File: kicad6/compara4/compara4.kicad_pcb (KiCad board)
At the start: 2 copper layers, 74.7 x 106.5 mm, 67 parts, among them J1 In_1, J2 In_2, J3 In_3, J4 In_4, J5 CV_Jack, J6 Out_OR, J7 Out_NOR, J8 Out_XOR, J9 Out_XNOR, Q1 BC547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

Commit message: notes, some design bits, state of progress
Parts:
- moved U3 151.7 mm to (248.9, 106.7)
- moved U2 139.4 mm to (248.9, 78.7)
- moved U1 127.0 mm to (248.9, 48.3)
- moved R14 74.2 mm to (193.6, 139.3)
- moved D5 74.2 mm to (197.3, 126.9)
- moved Q1 74.2 mm to (190.5, 152.4)
- moved Q2 74.2 mm to (219.7, 119.3)
- moved Q4 74.2 mm to (211.1, 131.4)
- moved R28 74.2 mm to (193.6, 135.3)
- moved R31 74.2 mm to (208.1, 127.2)
- moved R34 74.2 mm to (186.5, 127.2)
- moved Q3 74.2 mm to (205.2, 137.0)
- moved R11 74.2 mm to (186.5, 123.1)
- moved R13 74.2 mm to (208.1, 119.1)
- moved R15 74.2 mm to (186.5, 119.1)
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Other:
- board size 74.7 x 106.5 mm -> 239.4 x 106.5 mm

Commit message: compara4; breakout controls, layout for perfboard
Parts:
- removed D11: LED_XOR, LED_THT:LED_D3.0mm_FlatTop
- removed D12: LED_XNOR, LED_THT:LED_D3.0mm_FlatTop
- removed Q1, Q2, Q3, Q4: BC547, Package_TO_SOT_THT:TO-92_Inline
- removed R22, R23, R24: 10k, Resistor_THT:R_Axial_DIN0207_L6.3mm_D2.5mm_P7.62mm_Horizontal
- added C4: 10uF, Capacitor_THT:CP_Radial_D5.0mm_P2.50mm, F.Cu at (172.7, 129.6)
- added C5: 10uF, Capacitor_THT:CP_Radial_D5.0mm_P2.50mm, F.Cu at (172.7, 121.9)
- added J10: In_4, Connector_Audio:Jack_3.5mm_QingPu_WQP-PJ398SM_Vertical_CircularHoles, F.Cu at (86.4, 85.1)
- added J11: CV_Jack, Connector_Audio:Jack_3.5mm_QingPu_WQP-PJ398SM_Vertical_CircularHoles, F.Cu at (86.4, 54.6)
- added J12: Conn_02x05_Top_Bottom, Connector_IDC:IDC-Header_2x05_P2.54mm_Vertical, F.Cu at (182.9, 132.1)
- D10: value LED_NOR -> LED_Dual_Bidirectional; footprint LED_THT:LED_D3.0mm_FlatTop -> LED_THT:LED_D5.0mm
- D9: value LED_OR -> LED_Dual_Bidirectional; footprint LED_THT:LED_D3.0mm_FlatTop -> LED_THT:LED_D5.0mm
- J1: value In_1 -> Conn_01x34_Female; footprint Connector_Audio:Jack_3.5mm_QingPu_WQP-PJ398SM_Vertical_CircularHoles -> Connector_PinHeader_2.54mm:PinHeader_1x34_P2.54mm_Vertical; moved to B.Cu
- J2: value In_2 -> Conn_01x34_Male; footprint Connector_Audio:Jack_3.5mm_QingPu_WQP-PJ398SM_Vertical_CircularHoles -> Connector_PinHeader_2.54mm:PinHeader_1x34_P2.54mm_Horizontal; moved to B.Cu
- J3: value In_3 -> In_1
- J4: value In_4 -> In_2
- J5: value CV_Jack -> In_3
- J6: value Out_OR -> Out_XOR
- J7: value Out_NOR -> Out_XNOR
- J8: value Out_XOR -> Out_OR
- J9: value Out_XNOR -> Out_NOR
- R1: value 100k -> 10k
- R12: value 100k -> 47k
- R2, R21: value 10k -> 100k
- R7: value 47k -> 100k
- moved R12 131.4 mm to (68.6, 53.3), turned to -90 degrees
- moved R21 117.9 mm to (86.4, 40.6), turned to -90 degrees
- moved U3 112.1 mm to (139.7, 132.1), turned to 90 degrees
- moved R25 110.9 mm to (118.1, 119.4)
- moved R13 110.3 mm to (125.7, 45.7)
- moved U1 106.7 mm to (142.2, 45.7)
- moved R26 103.7 mm to (118.1, 134.6)
- moved R9 103.4 mm to (129.5, 55.9), turned to 90 degrees
- moved R14 94.0 mm to (134.6, 66.0)
- moved R17 89.8 mm to (133.3, 99.1), turned to 90 degrees
- moved R16 89.7 mm to (166.4, 45.7), turned to 180 degrees
- moved R2 89.5 mm to (118.1, 71.1), turned to 90 degrees
- moved D8 89.1 mm to (137.2, 96.5), turned to 90 degrees
- moved R3 88.7 mm to (123.2, 59.7), turned to -90 degrees
- moved U2 82.5 mm to (166.4, 78.7)
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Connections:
- D10 pad 1: Net-(D10-Pad1) -> /controls/LED_XOR_+
- D10 pad 2: Net-(D10-Pad2) -> /controls/LED_XOR_-
- D9 pad 1: Net-(D10-Pad2) -> /controls/LED_OR_+
- D9 pad 2: Net-(D10-Pad1) -> /controls/LED_OR_-
- J3 pad T: Net-(J3-PadT) -> /controls/IN1
- J4 pad T: Net-(J4-PadT) -> /controls/IN2
- J5 pad T: Net-(J5-PadT) -> /controls/IN3
- J5 pad TN: Net-(J5-PadTN) -> GND
- J6 pad T: Net-(J6-PadT) -> /controls/XOR
- J7 pad T: Net-(J7-PadT) -> /controls/XNOR
- J8 pad T: Net-(J8-PadT) -> /controls/OR
- J9 pad T: Net-(J9-PadT) -> /controls/NOR
- R1 pad 1: Net-(J5-PadTN) -> Net-(J2-Pad3)
- R12 pad 2: GND -> Net-(J11-PadT)
- R2 pad 2: Net-(J5-PadTN) -> Net-(J2-Pad3)
- R21 pad 1: Net-(Q1-Pad2) -> Net-(R12-Pad1)
- R21 pad 2: Net-(R21-Pad2) -> GND
- R25 pad 1: Net-(R25-Pad1) -> /LED_OR_-
- R25 pad 2: Net-(D10-Pad2) -> Net-(R25-Pad2)
- R26 pad 1: Net-(R26-Pad1) -> /LED_XOR_-
- R26 pad 2: Net-(D11-Pad1) -> Net-(R26-Pad2)
- R27 pad 1: Net-(J6-PadT) -> /OR
- R27 pad 2: Net-(Q1-Pad3) -> Net-(R27-Pad2)
- R28 pad 1: Net-(J7-PadT) -> /NOR
- R28 pad 2: Net-(Q2-Pad3) -> Net-(R28-Pad2)
- R29 pad 1: Net-(J6-PadT) -> /OR
- R3 pad 2: Net-(J1-PadT) -> Net-(J2-Pad11)
- R30 pad 1: Net-(J7-PadT) -> /NOR
- R31 pad 1: Net-(J8-PadT) -> /XOR
- R31 pad 2: Net-(Q3-Pad3) -> Net-(R31-Pad2)
- R32 pad 1: Net-(J9-PadT) -> /XNOR
- R32 pad 2: Net-(Q4-Pad3) -> Net-(R32-Pad2)
- R33 pad 1: Net-(J8-PadT) -> /XOR
- R34 pad 1: Net-(J9-PadT) -> /XNOR
- R4 pad 2: Net-(J2-PadT) -> Net-(J2-Pad12)
- R5 pad 2: Net-(J3-PadT) -> Net-(J2-Pad17)
- R6 pad 2: Net-(J4-PadT) -> Net-(J2-Pad18)
- R7 pad 1: Net-(R12-Pad1) -> Net-(D5-Pad1)
- R7 pad 2: Net-(J5-PadT) -> GND
- RV1 pad 2: Net-(RV1-Pad2) -> /controls/Threshold
- SW1 pad 1: +12V -> /controls/+12V
- SW1 pad 2: Net-(SW1-Pad2) -> /controls/Switch
- U1 pad 13: Net-(RV1-Pad2) -> /Threshold
- U1 pad 2: Net-(RV1-Pad2) -> /Threshold
- U1 pad 6: Net-(RV1-Pad2) -> /Threshold
- U1 pad 9: Net-(RV1-Pad2) -> /Threshold
- U2 pad 13: Net-(SW1-Pad2) -> /Switch
- U3 pad 1: Net-(D11-Pad2) -> /LED_XOR_+
- U3 pad 11: Net-(R21-Pad2) -> Net-(R27-Pad2)
- U3 pad 12: Net-(R22-Pad2) -> Net-(R28-Pad2)
- U3 pad 2: Net-(R26-Pad1) -> Net-(R26-Pad2)
- U3 pad 4: Net-(R23-Pad2) -> Net-(R31-Pad2)
- U3 pad 5: Net-(R24-Pad2) -> Net-(R32-Pad2)
- U3 pad 8: Net-(D10-Pad1) -> /LED_OR_+
- U3 pad 9: Net-(R25-Pad1) -> Net-(R25-Pad2)
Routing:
- net GND: track 0.00 -> 652.0 mm, vias 0 -> 6
- net +12V: track 0.00 -> 249.5 mm, vias 0 -> 2
- net -12V: track 0.00 -> 160.0 mm, vias 0 -> 2
- net /Switch: track 0.00 -> 100.3 mm
- net Net-(D5-Pad1): track 0.00 -> 88.9 mm, vias 0 -> 7
- net Net-(J2-Pad18): track 0.00 -> 88.9 mm
- net Net-(U2-Pad10): track 0.00 -> 86.4 mm, vias 0 -> 4
- net Net-(J2-Pad17): track 0.00 -> 76.2 mm
- net /Threshold: track 0.00 -> 58.4 mm
- net /LED_OR_+: track 0.00 -> 48.3 mm, vias 0 -> 1
- net Net-(D4-Pad1): track 0.00 -> 47.0 mm, vias 0 -> 3
- net Net-(D1-Pad1): track 0.00 -> 45.7 mm
- net Net-(D4-Pad2): track 0.00 -> 43.5 mm, vias 0 -> 4
- net Net-(D1-Pad2): track 0.00 -> 43.4 mm, vias 0 -> 2
- net Net-(R13-Pad1): track 0.00 -> 43.2 mm, vias 0 -> 4
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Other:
- board size 239.4 x 106.5 mm -> 124 x 106.5 mm

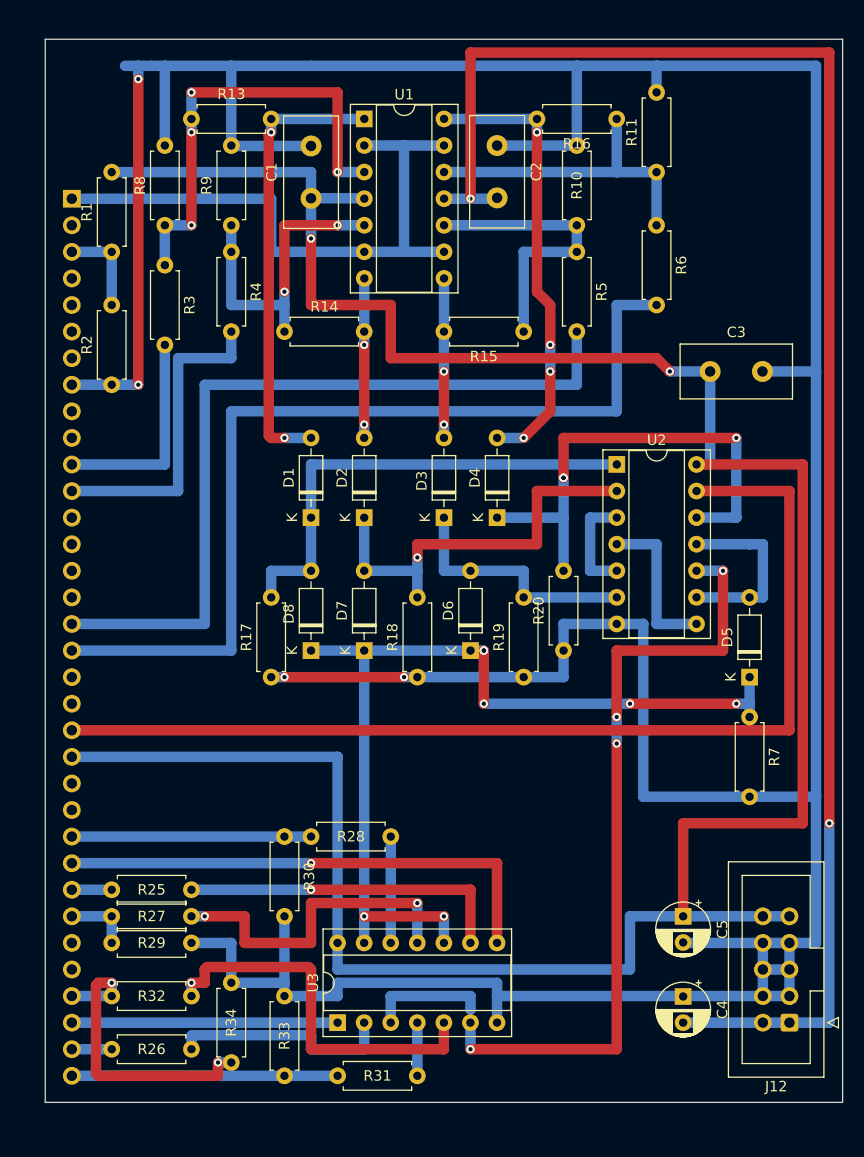
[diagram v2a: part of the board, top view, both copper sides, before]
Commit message: compara4 routing corrections: 2.54mm grid
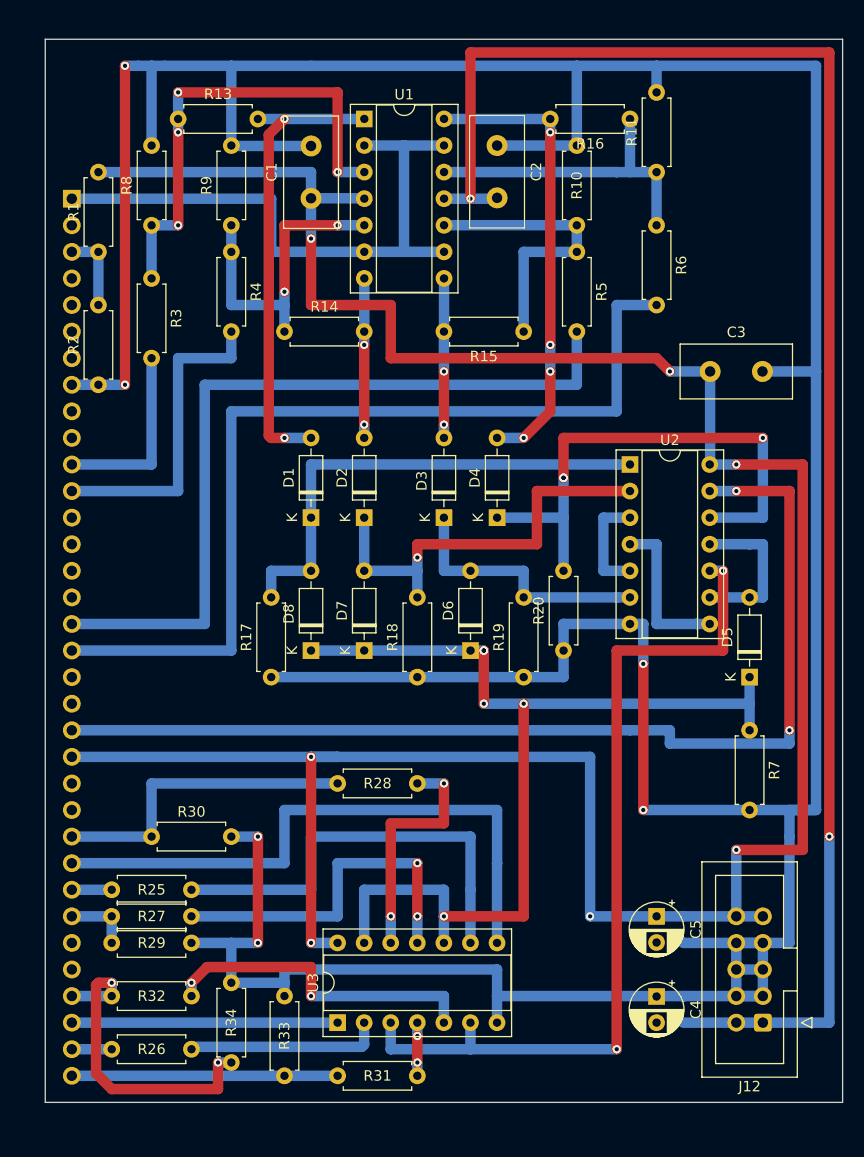
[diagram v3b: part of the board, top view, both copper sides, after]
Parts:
- moved R30 12.7 mm to (121.9, 114.3), turned to 0 degrees
- moved R28 5.68 mm to (139.7, 109.2)
- moved C4 2.54 mm to (170.2, 129.6)
- moved C5 2.54 mm to (170.2, 121.9)
- moved J12 2.54 mm to (180.3, 132.1)
- moved R3 1.80 mm to (121.9, 61.0)
- moved R13 1.27 mm to (124.5, 45.7)
- moved R1 1.27 mm to (116.8, 58.4)
- moved R2 1.27 mm to (116.8, 71.1)
- moved R7 1.27 mm to (179.1, 104.1)
- moved R8 1.27 mm to (121.9, 55.9)
- moved R16 1.27 mm to (167.6, 45.7)
- moved U2 1.26 mm to (167.6, 78.7)
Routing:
- net GND: track 652.0 -> 664.7 mm, vias 6 -> 8
- net Net-(R28-Pad2): track 10.2 -> 22.9 mm, vias 0 -> 2
- net Net-(R25-Pad2): track 31.8 -> 41.9 mm, vias 1 -> 0
- net /LED_OR_+: track 48.3 -> 58.4 mm, vias 1 -> 0
- net Net-(D5-Pad1): track 88.9 -> 97.8 mm, vias 7 -> 5
- net /NOR: track 22.9 -> 30.5 mm
- net Net-(R32-Pad2): track 37.0 -> 31.3 mm, vias 1 -> 2
- net Net-(D4-Pad1): track 47.0 -> 50.8 mm
- net +12V: track 249.5 -> 253.3 mm, vias 2 -> 7
- net Net-(R26-Pad2): track 21.7 -> 18.8 mm
- net Net-(R27-Pad2): track 31.7 -> 34.3 mm
- net Net-(R13-Pad1): track 43.2 -> 45.7 mm
- net Net-(J2-Pad11): track 20.3 -> 17.8 mm
- net Net-(U2-Pad10): track 86.4 -> 83.8 mm, vias 4 -> 2
- net Net-(D5-Pad2): track 17.8 -> 15.2 mm
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
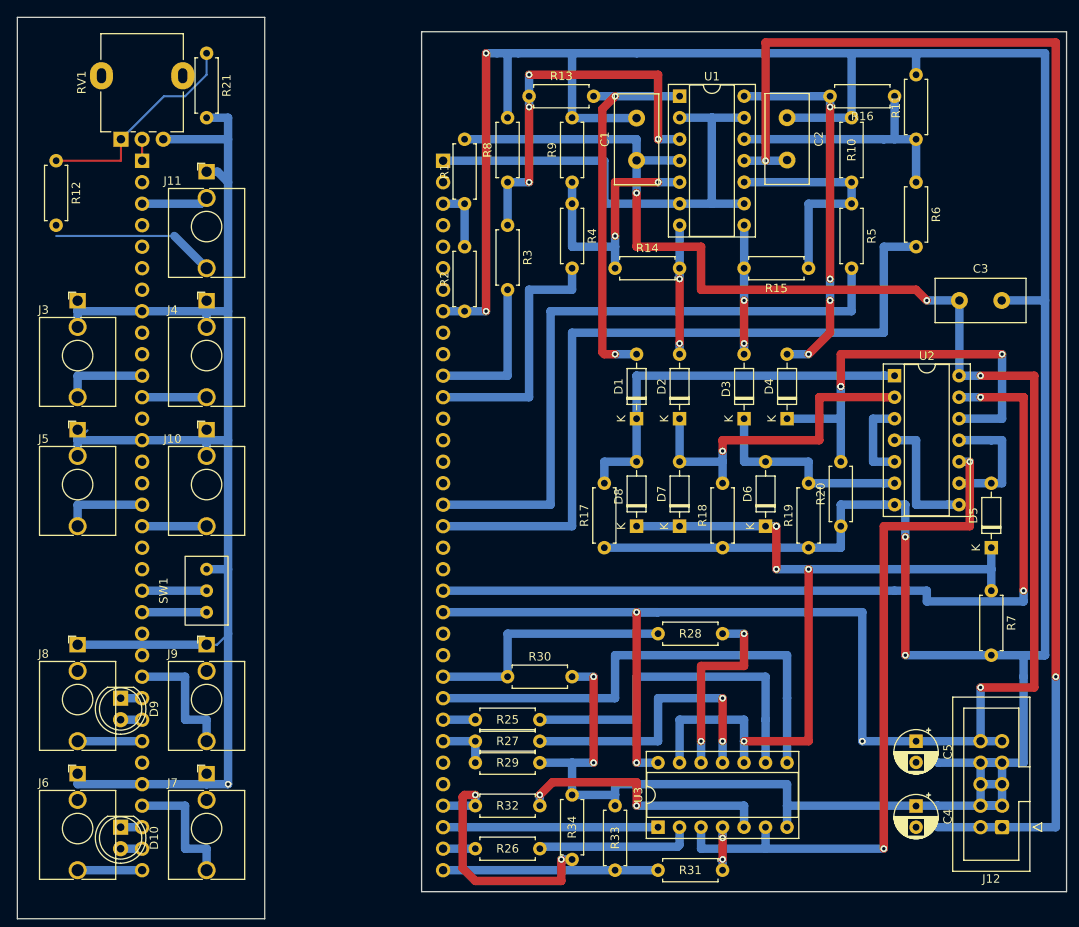
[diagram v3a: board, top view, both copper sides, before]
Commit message: compara4: reverse pot and cleanup ERC
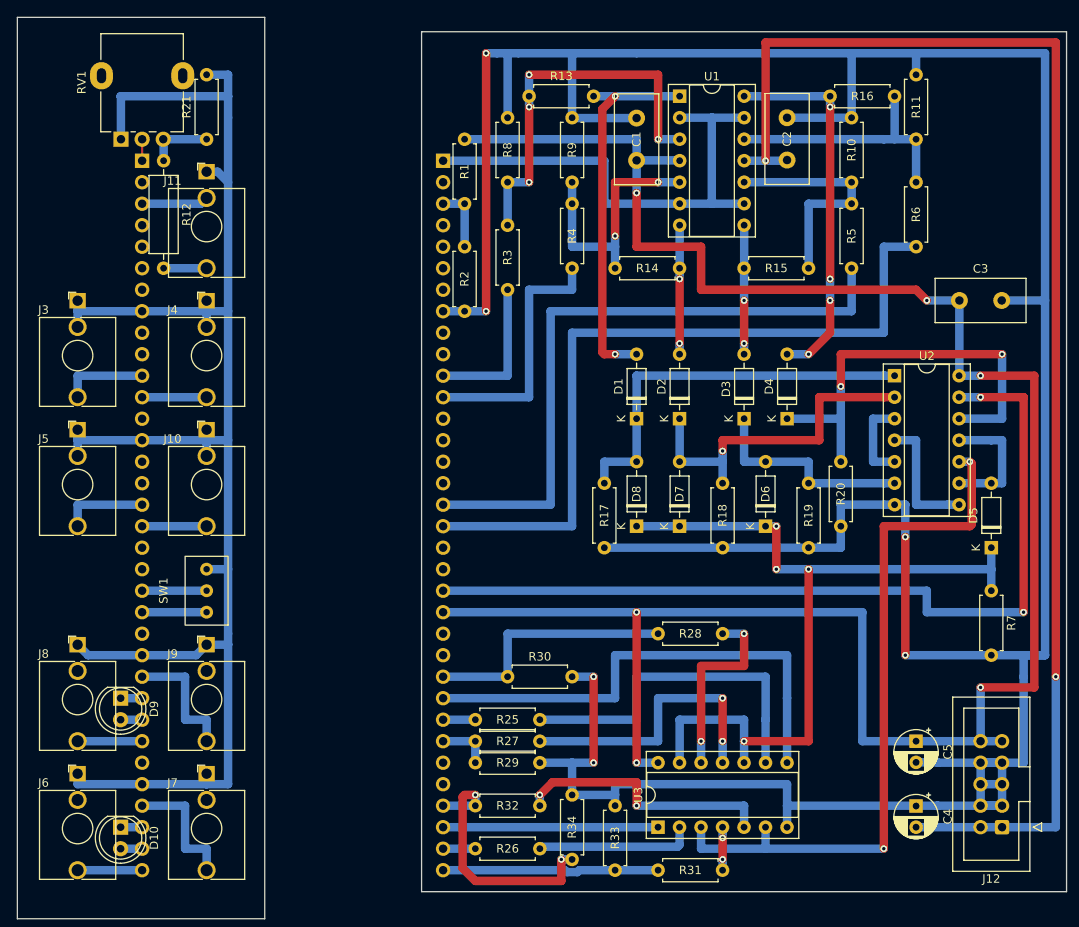
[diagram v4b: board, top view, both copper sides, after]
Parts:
- R12: footprint Resistor_THT:R_Axial_DIN0207_L6.3mm_D2.5mm_P7.62mm_Horizontal -> Resistor_THT:R_Axial_DIN0309_L9.0mm_D3.2mm_P12.70mm_Horizontal
- moved R12 12.7 mm to (81.3, 53.3)
- moved R21 10.2 mm to (86.4, 50.8), turned to 90 degrees
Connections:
- J1 pad 24: unconnected-(J1-Pad24) -> GND
- RV1 pad 1: Net-(R12-Pad1) -> GND
- RV1 pad 3: GND -> Net-(R12-Pad1)
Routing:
- net Net-(R12-Pad1): track 26.0 -> 7.68 mm, vias 1 -> 0
- net GND: track 664.7 -> 681.3 mm, vias 8 -> 6
- net Net-(J11-PadT): track 19.4 -> 5.08 mm
- net +12V: track 253.3 -> 250.8 mm, vias 7 -> 6
- net -12V: track 160.0 -> 162.6 mm
- net /Switch: track 101.6 -> 104.1 mm
- net Net-(D5-Pad1): vias 5 -> 4
- net Net-(D4-Pad1): vias 3 -> 2

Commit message: compara4; alignment corrections, some jumper cleanup
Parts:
- added R22: 10k, Resistor_THT:R_Axial_DIN0207_L6.3mm_D2.5mm_P7.62mm_Horizontal, F.Cu at (129.5, 106.7)
- R12: footprint Resistor_THT:R_Axial_DIN0309_L9.0mm_D3.2mm_P12.70mm_Horizontal -> Resistor_THT:R_Axial_DIN0207_L6.3mm_D2.5mm_P7.62mm_Horizontal
- moved R34 17.6 mm to (114.3, 127.0), turned to 0 degrees
- moved R13 15.5 mm to (139.7, 43.2), turned to 180 degrees
- moved R3 10.2 mm to (121.9, 71.1)
- moved R33 5.08 mm to (129.5, 137.2)
- moved R25 3.81 mm to (114.3, 119.4)
- moved R26 3.81 mm to (114.3, 134.6)
- moved R27 3.81 mm to (114.3, 121.9)
- moved R29 3.81 mm to (114.3, 124.5)
- moved R32 3.81 mm to (114.3, 129.5)
- moved R7 2.84 mm to (180.3, 101.6)
- moved R20 2.84 mm to (160.0, 94.0)
- moved R1 2.54 mm to (114.3, 58.4)
- moved R15 2.54 mm to (157.5, 63.5)
- moved R2 2.54 mm to (114.3, 71.1)
- moved R16 2.54 mm to (167.6, 43.2)
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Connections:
- J2 pad 22: +12V -> Net-(J2-Pad22)
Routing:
- net /XNOR: track 31.2 -> 5.08 mm, vias 2 -> 0
- net Net-(R13-Pad1): track 45.7 -> 66.0 mm, vias 4 -> 2
- net +12V: track 250.8 -> 236.2 mm, vias 6 -> 8
- net Net-(J2-Pad22): track 0.00 -> 10.2 mm
- net Net-(J2-Pad11): track 17.8 -> 10.2 mm
- net Net-(J2-Pad17): track 76.2 -> 83.8 mm, vias 0 -> 2
- net GND: track 681.3 -> 687.7 mm
- net Net-(R11-Pad1): track 30.5 -> 35.6 mm
- net Net-(J2-Pad18): track 88.9 -> 94.0 mm, vias 0 -> 2
- net Net-(D2-Pad2): track 15.2 -> 20.3 mm
- net Net-(R26-Pad2): track 18.8 -> 22.9 mm
- net Net-(D4-Pad2): track 44.2 -> 48.3 mm, vias 4 -> 2
- net Net-(R27-Pad2): track 34.3 -> 38.1 mm
- net Net-(R25-Pad2): track 41.9 -> 45.7 mm
- net /Switch: track 104.1 -> 101.6 mm
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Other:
- board size 124 x 106.5 mm -> 124 x 107.3 mm
